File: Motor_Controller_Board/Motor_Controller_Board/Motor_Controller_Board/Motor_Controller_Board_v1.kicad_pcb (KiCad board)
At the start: 2 copper layers, 92 parts, among them J201 Conn_01x02, J202 Conn_01x02, J301 Conn_01x04, J302 USB_B_Micro, J303 Conn_01x02, J304 Conn_01x02, J305 Conn_01x02, J401 Conn_01x04, J402 Conn_01x04, J403 Conn_01x04, SW301 SW_Push, SW302 SW_Push, U201 TP6841S6, U301 AMS1117, U302 ESP32-C6-MINI-1, U401 A4988, U402 A4988, U403 A4988

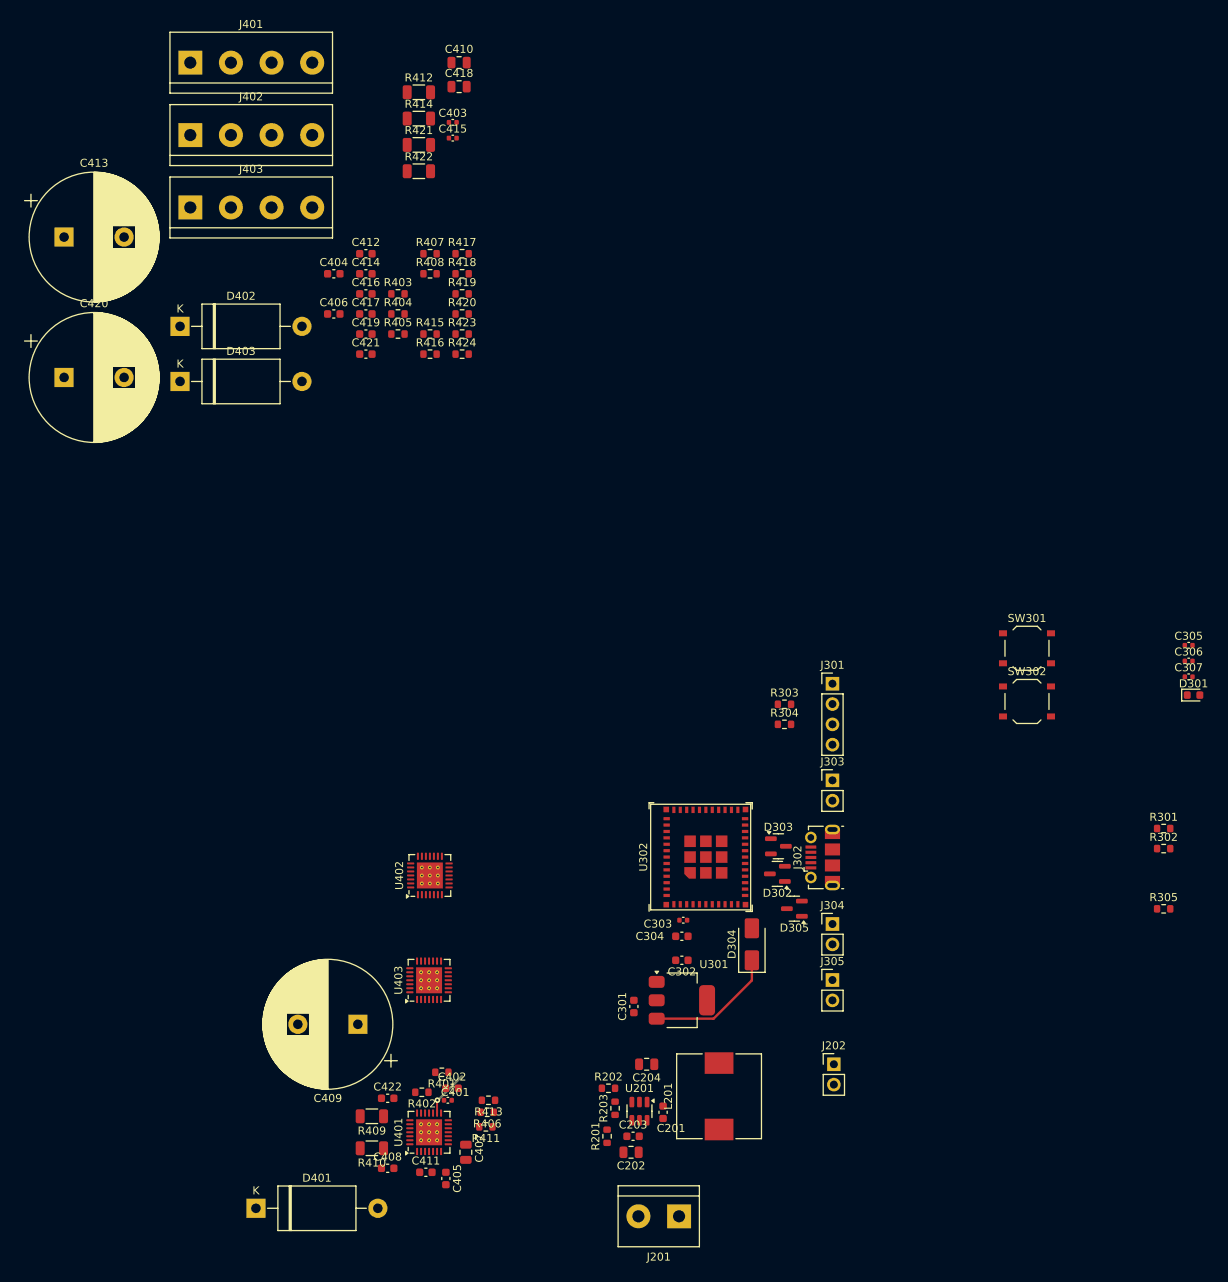
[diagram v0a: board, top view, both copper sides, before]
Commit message: discussed with Alex and Mishari. confident in schematic, going to do layout tomorrow
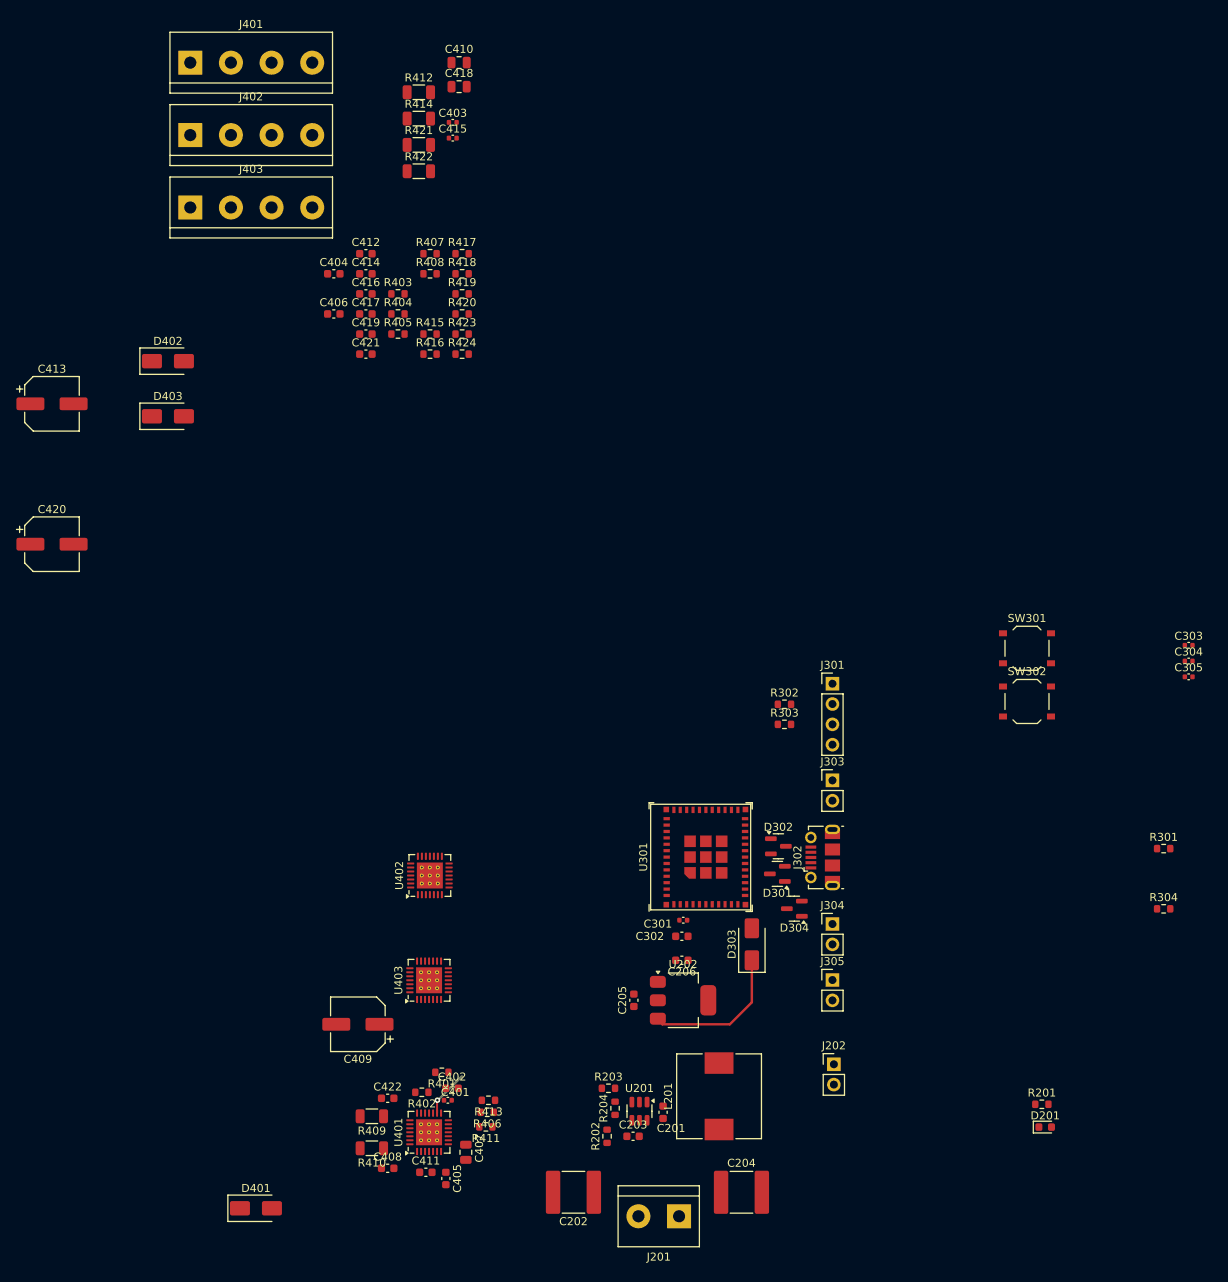
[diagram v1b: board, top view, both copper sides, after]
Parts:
- removed the C301 at (173.0, 124.8)
- removed the C302 at (179.0, 119.0)
- removed the D301 at (243.0, 85.8)
- removed the R301 at (239.2, 102.5)
- removed the U301 at (179.0, 124.0)
- added C205: 22u, Capacitor_SMD:C_0603_1608Metric, F.Cu at (173.0, 124.0)
- added C206: 22u, Capacitor_SMD:C_0603_1608Metric, F.Cu at (179.0, 119.0)
- added D201: RED, LED_SMD:LED_0603_1608Metric, F.Cu at (224.4, 139.8)
- added R201: 5k1, Resistor_SMD:R_0603_1608Metric, F.Cu at (224.0, 137.0)
- added U202: AMS1117, Package_TO_SOT_SMD:SOT-223-3_TabPin2, F.Cu at (179.2, 124.0)
- C202, C204: value 10u -> 22u; footprint Capacitor_SMD:C_0805_2012Metric -> Capacitor_SMD:C_2220_5750Metric
- C409, C413, C420: footprint Capacitor_THT:CP_Radial_D16.0mm_P7.50mm -> Capacitor_SMD:CP_Elec_6.3x7.7
- D401, D402, D403: value IN5402 -> SMAJ28A; footprint Diode_THT:D_DO-27_P15.24mm_Horizontal -> Diode_SMD:D_SMA
- moved C413 20.9 mm to (100.3, 49.4)
- moved C420 20.9 mm to (100.3, 67.0)
- moved C204 19.9 mm to (186.4, 148.0), turned to 0 degrees
- moved C202 8.77 mm to (165.4, 148.0)
- moved D402 4.61 mm to (114.8, 44.1)
- moved D403 4.61 mm to (114.8, 51.0)
- renumbered C303 to C301, C304 to C302, C305 to C303, C306 to C304, C307 to C305, D302 to D301, D303 to D302, D304 to D303, D305 to D304, R201 to R202, R202 to R203, R203 to R204, R302 to R301, R303 to R302, R304 to R303, R305 to R304, U302 to U301
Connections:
- net +3.3V renamed VCC
- D403 pad 1: /Stepper Drivers/V_FLYBACK -> /Stepper Drivers/A_FLYBACK
- R419 pad 2: /Stepper Drivers/V_FLYBACK -> /Stepper Drivers/A_FLYBACK
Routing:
- net +5V: track 16.4 -> 18.6 mm

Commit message: general placement done. discuss with teammates tomorrow
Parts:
- added C423: 100u, Capacitor_SMD:CP_Elec_6.3x7.7, F.Cu at (138.0, 118.0)
- added C424: 100n, Capacitor_SMD:C_0603_1608Metric, F.Cu at (147.0, 114.0)
- C409, C413: value 100u -> 100n; footprint Capacitor_SMD:CP_Elec_6.3x7.7 -> Capacitor_SMD:C_0603_1608Metric
- C410: value 220n -> 100u; footprint Capacitor_SMD:C_0805_2012Metric -> Capacitor_SMD:CP_Elec_6.3x7.7
- C411: value 100n -> 220n; footprint Capacitor_SMD:C_0603_1608Metric -> Capacitor_SMD:C_0805_2012Metric
- C415: value 100n -> 100u; footprint Capacitor_SMD:C_0402_1005Metric -> Capacitor_SMD:CP_Elec_6.3x7.7
- C416: value 22u -> 100n
- C417: footprint Capacitor_SMD:C_0603_1608Metric -> Capacitor_SMD:C_0402_1005Metric
- C418: value 220n -> 22u; footprint Capacitor_SMD:C_0805_2012Metric -> Capacitor_SMD:C_0603_1608Metric
- C420: value 100u -> 220n; footprint Capacitor_SMD:CP_Elec_6.3x7.7 -> Capacitor_SMD:C_0805_2012Metric
- D401, D402, D403: value SMAJ28A -> SMAJ22A
- R405, R407, R419: value 10k -> 10R
- moved C415 131.9 mm to (138.3, 147.6), turned to 180 degrees
- moved R414 126.9 mm to (141.0, 140.6), turned to 180 degrees
- moved R412 126.2 mm to (141.0, 136.6), turned to 180 degrees
- moved C403 119.8 mm to (149.5, 134.1), turned to 180 degrees
- moved R407 118.0 mm to (145.0, 148.6), turned to -90 degrees
- moved J402 115.1 mm to (124.0, 130.8), turned to -90 degrees
- moved D402 112.6 mm to (141.0, 153.6), turned to 180 degrees
- moved C416 108.2 mm to (147.2, 143.6)
- moved C406 106.9 mm to (150.0, 144.1), turned to -90 degrees
- moved R408 104.0 mm to (154.2, 137.0), turned to 180 degrees
- moved C413 102.1 mm to (142.0, 142.6)
- moved C414 101.5 mm to (142.0, 134.6)
- moved C404 100.5 mm to (150.2, 132.6)
- moved R415 98.0 mm to (154.2, 138.5), turned to 180 degrees
- moved R403 94.4 mm to (148.0, 130.0), turned to 180 degrees
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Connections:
- net VCC renamed +3.3V
- C409 pad 1: +24V -> GND
- C409 pad 2: GND -> +24V
- C410 pad 1: /Stepper Drivers/H_VREG -> +24V
- C411 pad 1: /Stepper Drivers/A_CP1 -> /Stepper Drivers/H_VREG
- C411 pad 2: /Stepper Drivers/A_CP2 -> GND
- C412 pad 1: GND -> /Stepper Drivers/A_CP1
- C412 pad 2: +24V -> /Stepper Drivers/A_CP2
- C413 pad 1: +24V -> GND
- C413 pad 2: GND -> +24V
- C414 pad 1: /Stepper Drivers/H_CP1 -> GND
- C414 pad 2: /Stepper Drivers/H_CP2 -> +24V
- C415 pad 1: GND -> +24V
- C415 pad 2: +5V -> GND
- C416 pad 1: +5V -> /Stepper Drivers/H_CP1
- C416 pad 2: GND -> /Stepper Drivers/H_CP2
- C417 pad 1: /Stepper Drivers/V_VCP -> GND
- C417 pad 2: +24V -> +5V
- C418 pad 1: /Stepper Drivers/V_VREG -> +5V
- C419 pad 1: GND -> /Stepper Drivers/V_VCP
- C420 pad 1: +24V -> /Stepper Drivers/V_VREG
- C421 pad 1: /Stepper Drivers/V_CP1 -> GND
- C421 pad 2: /Stepper Drivers/V_CP2 -> +24V
- D403 pad 1: /Stepper Drivers/A_FLYBACK -> /Stepper Drivers/V_FLYBACK
- J401 pad 1: /Stepper Drivers/AGITATE_1A -> /Stepper Drivers/AGITATE_1B
- J401 pad 2: /Stepper Drivers/AGITATE_1B -> /Stepper Drivers/AGITATE_1A
- J402 pad 1: /Stepper Drivers/HORIZONTAL_1A -> /Stepper Drivers/HORIZONTAL_1B
- J402 pad 2: /Stepper Drivers/HORIZONTAL_1B -> /Stepper Drivers/HORIZONTAL_1A
- J403 pad 1: /Stepper Drivers/VERTICAL_1A -> /Stepper Drivers/VERTICAL_1B
- J403 pad 2: /Stepper Drivers/VERTICAL_1B -> /Stepper Drivers/VERTICAL_1A
- R401 pad 1: +5V -> /Stepper Drivers/A_VREF
- R401 pad 2: /Stepper Drivers/A_VREF -> +5V
- R419 pad 2: /Stepper Drivers/A_FLYBACK -> /Stepper Drivers/V_FLYBACK
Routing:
- net AGITATION_STEP: track 5.92 -> 0.00 mm, vias 1 -> 0

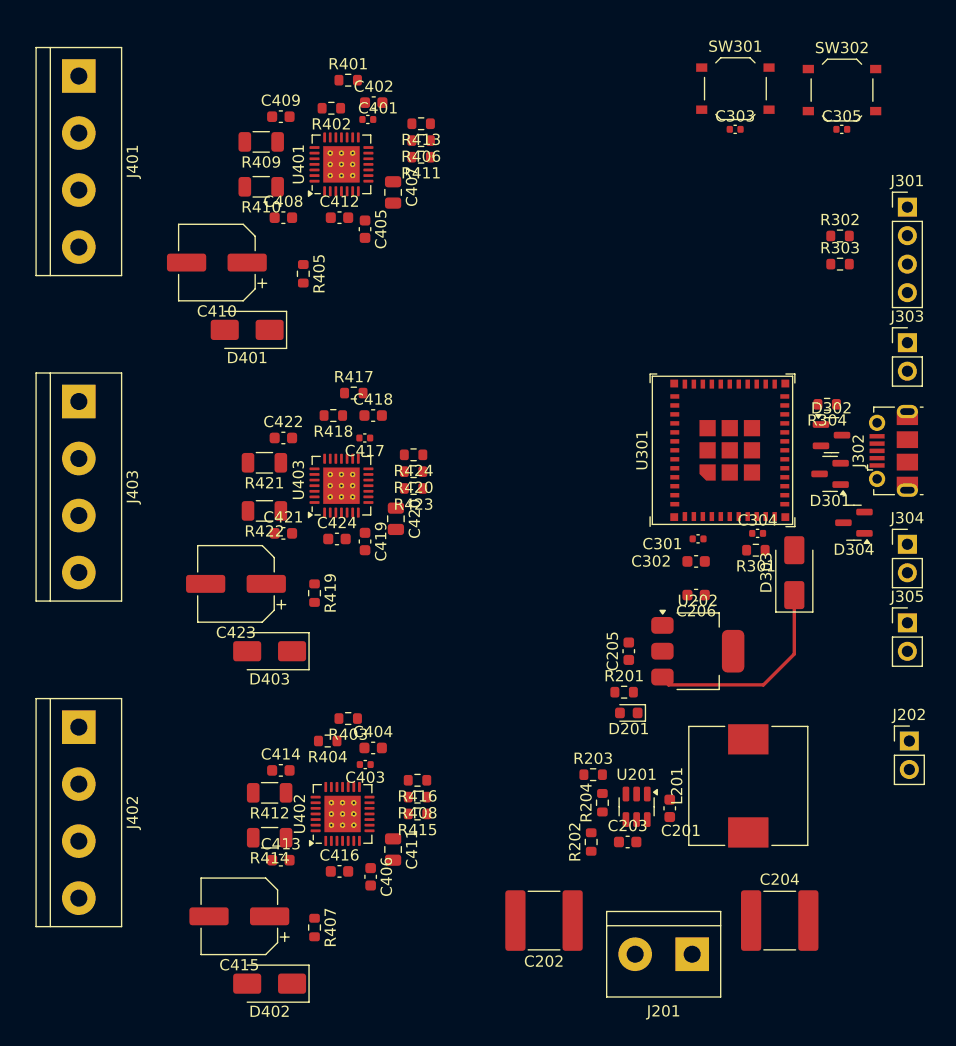
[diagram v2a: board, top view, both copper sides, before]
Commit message: routing 75% finished, but very sloppy
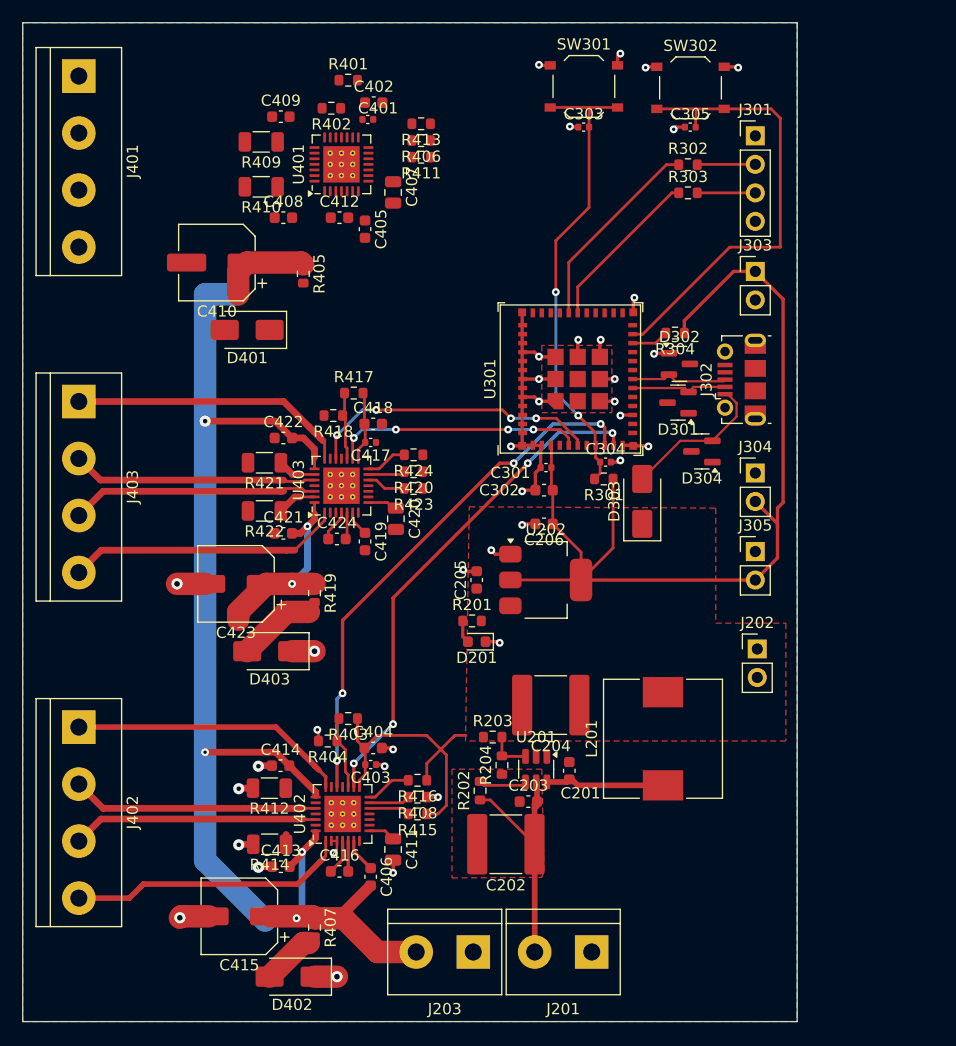
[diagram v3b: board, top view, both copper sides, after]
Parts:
- added J203: Conn_01x02, TerminalBlock:TerminalBlock_bornier-2_P5.08mm, F.Cu at (159.1, 150.8)
- D401, D402, D403: value SMAJ22A -> SMAJ28A
- R405, R407, R419: value 10R -> 10k
- moved C204 28.0 mm to (166.1, 128.8), turned to 180 degrees
- moved J202 15.8 mm to (184.4, 123.8)
- moved D301 15.0 mm to (177.4, 101.8)
- moved J302 15.0 mm to (183.0, 99.8)
- moved R201 15.0 mm to (159.0, 121.3)
- moved C205 15.0 mm to (159.4, 117.7)
- moved C206 15.0 mm to (165.4, 112.7)
- moved C301 15.0 mm to (165.6, 107.6)
- moved C302 15.0 mm to (165.4, 109.7)
- moved D201 15.0 mm to (159.4, 123.2)
- moved D302 15.0 mm to (177.5, 98.4)
- moved D303 15.0 mm to (174.2, 110.7)
- moved D304 15.0 mm to (179.5, 106.2)
- moved R304 15.0 mm to (177.1, 95.7)
- moved U202 15.0 mm to (165.6, 117.7)
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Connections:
- C202 pad 1: +24V -> /Power Supply/DIGITAL_POWER_+24V
- C203 pad 2: +24V -> /Power Supply/DIGITAL_POWER_+24V
- D401 pad 1: /Stepper Drivers/A_FLYBACK -> GND
- D401 pad 2: GND -> /Stepper Drivers/A_FLYBACK
- D402 pad 1: /Stepper Drivers/H_FLYBACK -> GND
- D402 pad 2: GND -> /Stepper Drivers/H_FLYBACK
- D403 pad 1: /Stepper Drivers/V_FLYBACK -> GND
- D403 pad 2: GND -> /Stepper Drivers/V_FLYBACK
- J201 pad 2: +24V -> /Power Supply/DIGITAL_POWER_+24V
- R202 pad 1: +24V -> /Power Supply/DIGITAL_POWER_+24V
- U201 pad 5: +24V -> /Power Supply/DIGITAL_POWER_+24V
- U301 pad 10: unconnected-(U301-IO5-Pad10) -> HORIZONTAL_STEP
- U301 pad 26: HORIZONTAL_DIR -> unconnected-(U301-IO20-Pad26)
- U301 pad 27: HORIZONTAL_STEP -> unconnected-(U301-IO21-Pad27)
- U301 pad 28: VERTICAL_DIR -> unconnected-(U301-IO22-Pad28)
- U301 pad 29: VERTICAL_STEP -> unconnected-(U301-IO23-Pad29)
- U301 pad 5: unconnected-(U301-IO2-Pad5) -> VERTICAL_STEP
- U301 pad 6: unconnected-(U301-IO3-Pad6) -> VERTICAL_DIR
- U301 pad 9: unconnected-(U301-IO4-Pad9) -> HORIZONTAL_DIR
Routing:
- net +24V: track 0.00 -> 140.0 mm, vias 0 -> 6
- net +3.3V: track 0.00 -> 87.1 mm
- net GND: track 0.00 -> 75.2 mm, vias 0 -> 38
- net HORIZONTAL_DIR: track 0.00 -> 47.4 mm, vias 0 -> 4
- net HORIZONTAL_STEP: track 0.00 -> 44.8 mm, vias 0 -> 4
- net /Microcontroller/EN: track 0.00 -> 42.2 mm, vias 0 -> 2
- net /Microcontroller/BOOT: track 0.00 -> 40.8 mm
- net VERTICAL_DIR: track 0.00 -> 26.3 mm, vias 0 -> 4
- net /Stepper Drivers/HORIZONTAL_1B: track 0.00 -> 25.3 mm
- net /Stepper Drivers/HORIZONTAL_2B: track 0.00 -> 25.3 mm
- net /Stepper Drivers/VERTICAL_1B: track 0.00 -> 25.2 mm
- net /Stepper Drivers/VERTICAL_2B: track 0.00 -> 24.5 mm
- net /Power Supply/DIGITAL_POWER_+24V: track 0.00 -> 22.5 mm
- net /Stepper Drivers/HORIZONTAL_2A: track 0.00 -> 22.4 mm
- net /Stepper Drivers/VERTICAL_1A: track 0.00 -> 22.4 mm
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- added copper zone on F.Cu, net +24V
- added copper zone on F.Cu, net +5V
- added copper zone on B.Cu, net GND
- added copper zone on F.Cu, net GND
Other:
- board outline added: 69 x 89 mm
